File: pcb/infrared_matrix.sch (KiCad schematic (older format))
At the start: 2 parts, among them U2 CD4051B

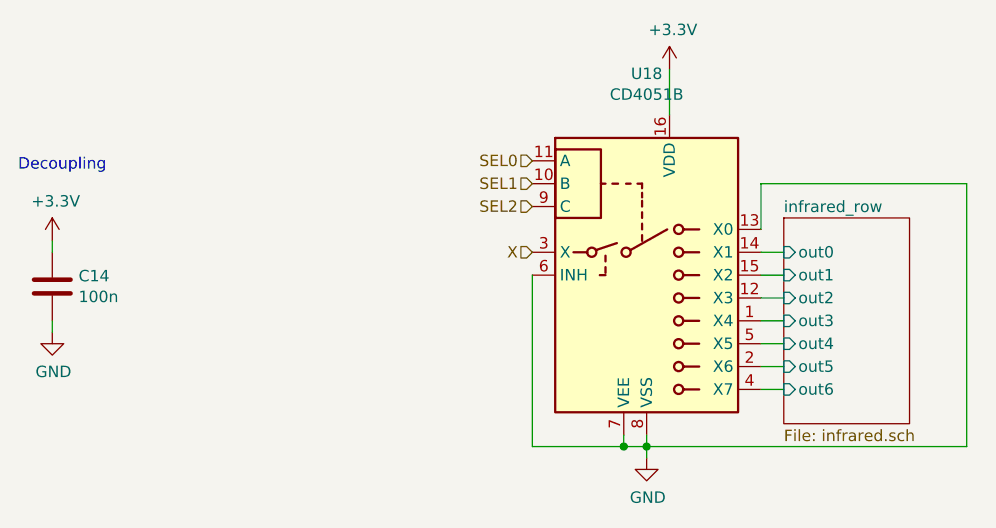
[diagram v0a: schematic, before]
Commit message: Infrared index starts at 0
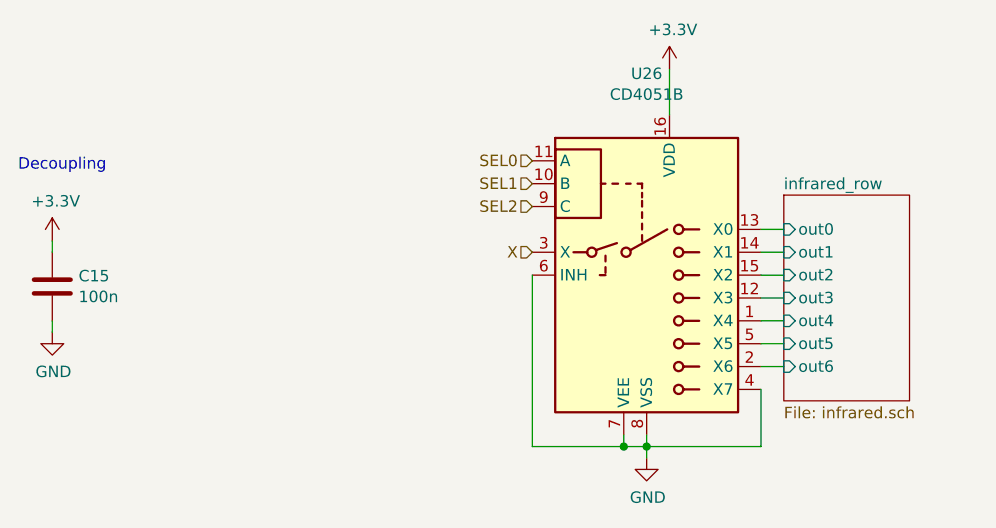
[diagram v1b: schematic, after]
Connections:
- net GND: now also U2.4 (X7); no longer U2.13 (X0)
- net infrared_row/out0: now also U2.13 (X0); no longer U2.14 (X1)
- net infrared_row/out1: now also U2.14 (X1); no longer U2.15 (X2)
- net infrared_row/out2: now also U2.15 (X2); no longer U2.12 (X3)
- net infrared_row/out3: now also U2.12 (X3); no longer U2.1 (X4)
- net infrared_row/out4: now also U2.1 (X4); no longer U2.5 (X5)
- net infrared_row/out5: now also U2.5 (X5); no longer U2.2 (X6)
- net infrared_row/out6: now also U2.2 (X6); no longer U2.4 (X7)
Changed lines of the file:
@@
 $Descr A4 11693 8268
 encoding utf-8
-Sheet 8 17
+Sheet 10 17
 Title ""
 Date ""
@@
 $EndDescr
 $Sheet
-S 6000 3550 550  900
+S 6000 3450 550  900
 U 5D2943E6
 F0 "infrared_row" 50
 F1 "infrared.sch" 50
-F2 "out0" I L 6000 3700 50
-F3 "out1" I L 6000 3800 50
-F4 "out3" I L 6000 4000 50
-F5 "out2" I L 6000 3900 50
-F6 "out4" I L 6000 4100 50
-F7 "out5" I L 6000 4200 50
-F8 "out6" I L 6000 4300 50
+F2 "out0" I L 6000 3600 50
+F3 "out1" I L 6000 3700 50
+F4 "out3" I L 6000 3900 50
+F5 "out2" I L 6000 3800 50
+F6 "out4" I L 6000 4000 50
+F7 "out5" I L 6000 4100 50
+F8 "out6" I L 6000 4200 50
 $EndSheet
 $Comp
@@
 AR Path="/5D1373A3/5D2E89D4/5D29B58C" Ref="U42"  Part="1"
 AR Path="/5D1373A3/5D2E8A06/5D29B58C" Ref="U50"  Part="1"
-F 0 "U18" H 5400 4681 50  0000 C CNN
+F 0 "U26" H 5400 4681 50  0000 C CNN
 F 1 "CD4051B" H 5400 4590 50  0000 C CNN
 F 2 "Package_SO:SOP-16_4.55x10.3mm_P1.27mm" H 5550 3050 50  0001 L CNN
@@
 AR Path="/5D1373A3/5D2E89D4/5D2C5607" Ref="#PWR0114"  Part="1"
 AR Path="/5D1373A3/5D2E8A06/5D2C5607" Ref="#PWR0133"  Part="1"
-F 0 "#PWR057" H 5500 2750 50  0001 C CNN
+F 0 "#PWR076" H 5500 2750 50  0001 C CNN
 F 1 "+3.3V" H 5515 3073 50  0000 C CNN
 F 2 "" H 5500 2900 50  0001 C CNN
@@
 AR Path="/5D1373A3/5D2E89D4/5D2C6E9F" Ref="#PWR0116"  Part="1"
 AR Path="/5D1373A3/5D2E8A06/5D2C6E9F" Ref="#PWR0135"  Part="1"
-F 0 "#PWR059" H 5400 4350 50  0001 C CNN
+F 0 "#PWR078" H 5400 4350 50  0001 C CNN
 F 1 "GND" H 5405 4427 50  0000 C CNN
 F 2 "" H 5400 4600 50  0001 C CNN
@@
 X
 Wire Wire Line
+	5900 3800 6000 3800
+Wire Wire Line
 	5900 3900 6000 3900
 Wire Wire Line
@@
 	5900 4100 6000 4100
 Wire Wire Line
-	5900 4200 6000 4200
-Wire Wire Line
-	6000 4300 5900 4300
+	6000 4200 5900 4200
 Wire Wire Line
 	5300 4550 5400 4550
@@
 AR Path="/5D1373A3/5D2E89D4/5D2F8064" Ref="#PWR0115"  Part="1"
 AR Path="/5D1373A3/5D2E8A06/5D2F8064" Ref="#PWR0134"  Part="1"
-F 0 "#PWR058" H 2800 3500 50  0001 C CNN
+F 0 "#PWR077" H 2800 3500 50  0001 C CNN
 F 1 "+3.3V" H 2815 3823 50  0000 C CNN
 F 2 "" H 2800 3650 50  0001 C CNN
@@
 AR Path="/5D1373A3/5D2E8934/5D2F9ADC" Ref="C15"  Part="1"
 AR Path="/5D1373A3/5D2E8986/5D2F9ADC" Ref="C16"  Part="1"
-F 0 "C14" H 2915 3896 50  0000 L CNN
+F 0 "C15" H 2915 3896 50  0000 L CNN
 F 1 "100n" H 2915 3805 50  0000 L CNN
 F 2 "Capacitor_SMD:C_0805_2012Metric" H 2838 3700 50  0001 C CNN
@@
 $EndComp
 Wire Wire Line
-	5900 3600 5900 3400
-Wire Wire Line
-	5900 3800 6000 3800
-Wire Wire Line
-	6800 4550 5400 4550
-Wire Wire Line
-	5900 3400 6800 3400
-Wire Wire Line
-	6800 3400 6800 4550
-Wire Wire Line
 	5900 3700 6000 3700
+Wire Wire Line
+	5900 3600 6000 3600
 Text HLabel 4900 3300 0    50   Input ~ 0
 SEL0
@@
 AR Path="/5D1373A3/5D2E89D4/5D310C2B" Ref="#PWR0157"  Part="1"
 AR Path="/5D1373A3/5D2E8A06/5D310C2B" Ref="#PWR0158"  Part="1"
-F 0 "#PWR0154" H 2800 3800 50  0001 C CNN
+F 0 "#PWR0155" H 2800 3800 50  0001 C CNN
 F 1 "GND" H 2805 3877 50  0000 C CNN
 F 2 "" H 2800 4050 50  0001 C CNN
@@
 Text Notes 2650 3350 0    50   ~ 0
 Decoupling
+Wire Wire Line
+	5900 4300 5900 4550
+Wire Wire Line
+	5900 4550 5400 4550
 $EndSCHEMATC

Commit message: Use Buses for IR sensors
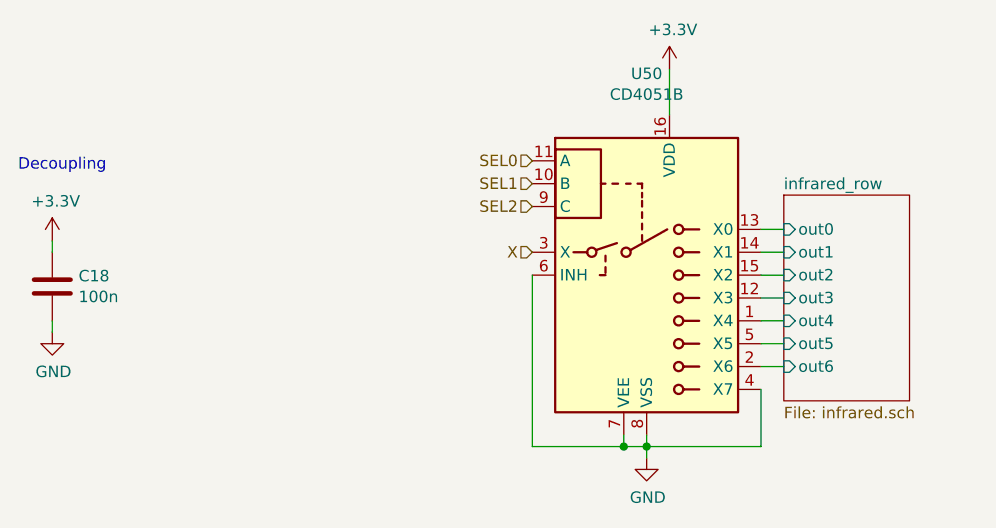
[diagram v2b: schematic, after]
